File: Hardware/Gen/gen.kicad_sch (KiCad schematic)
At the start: 51 parts, among them J1 Screw_Terminal_01x03, J2 XLR4, J3 XLR3, J4 GAMEN, J5 SHORI, J6 MAE, J7 Screw_Terminal_01x02, U1 TPS56339DDCT, U3 TPS560430YDBVR

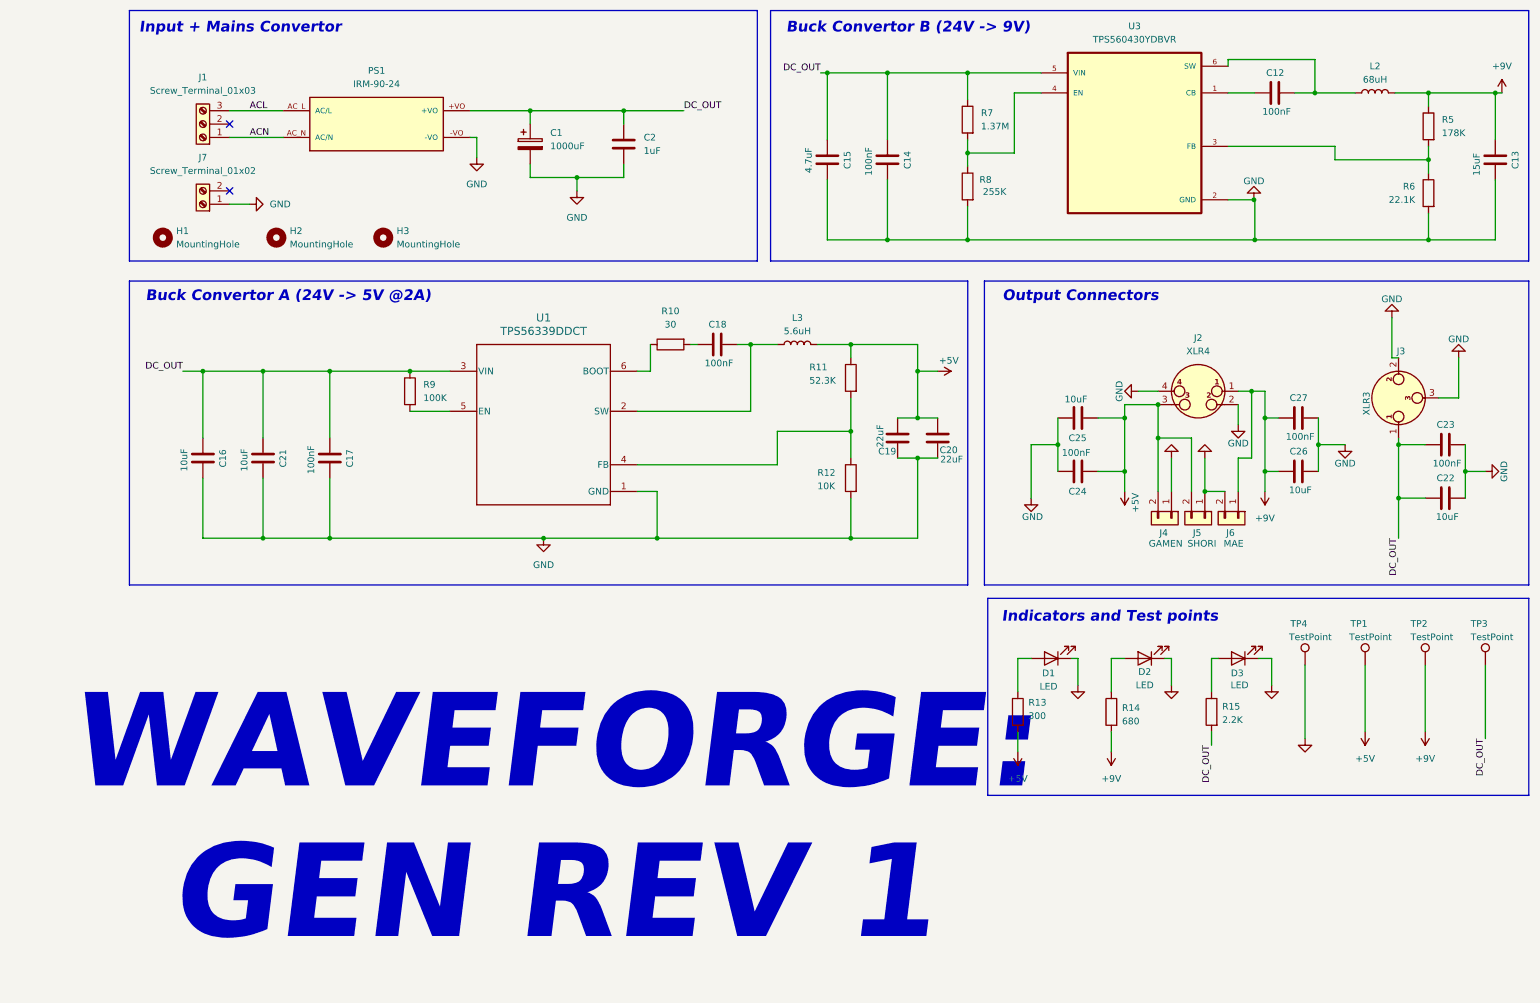
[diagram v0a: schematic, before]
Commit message: Gen: 5V buck convertor rework schems
Changed the 5V buck convertor to fgollow a ti chip with more of a max voltage headroom for safety.
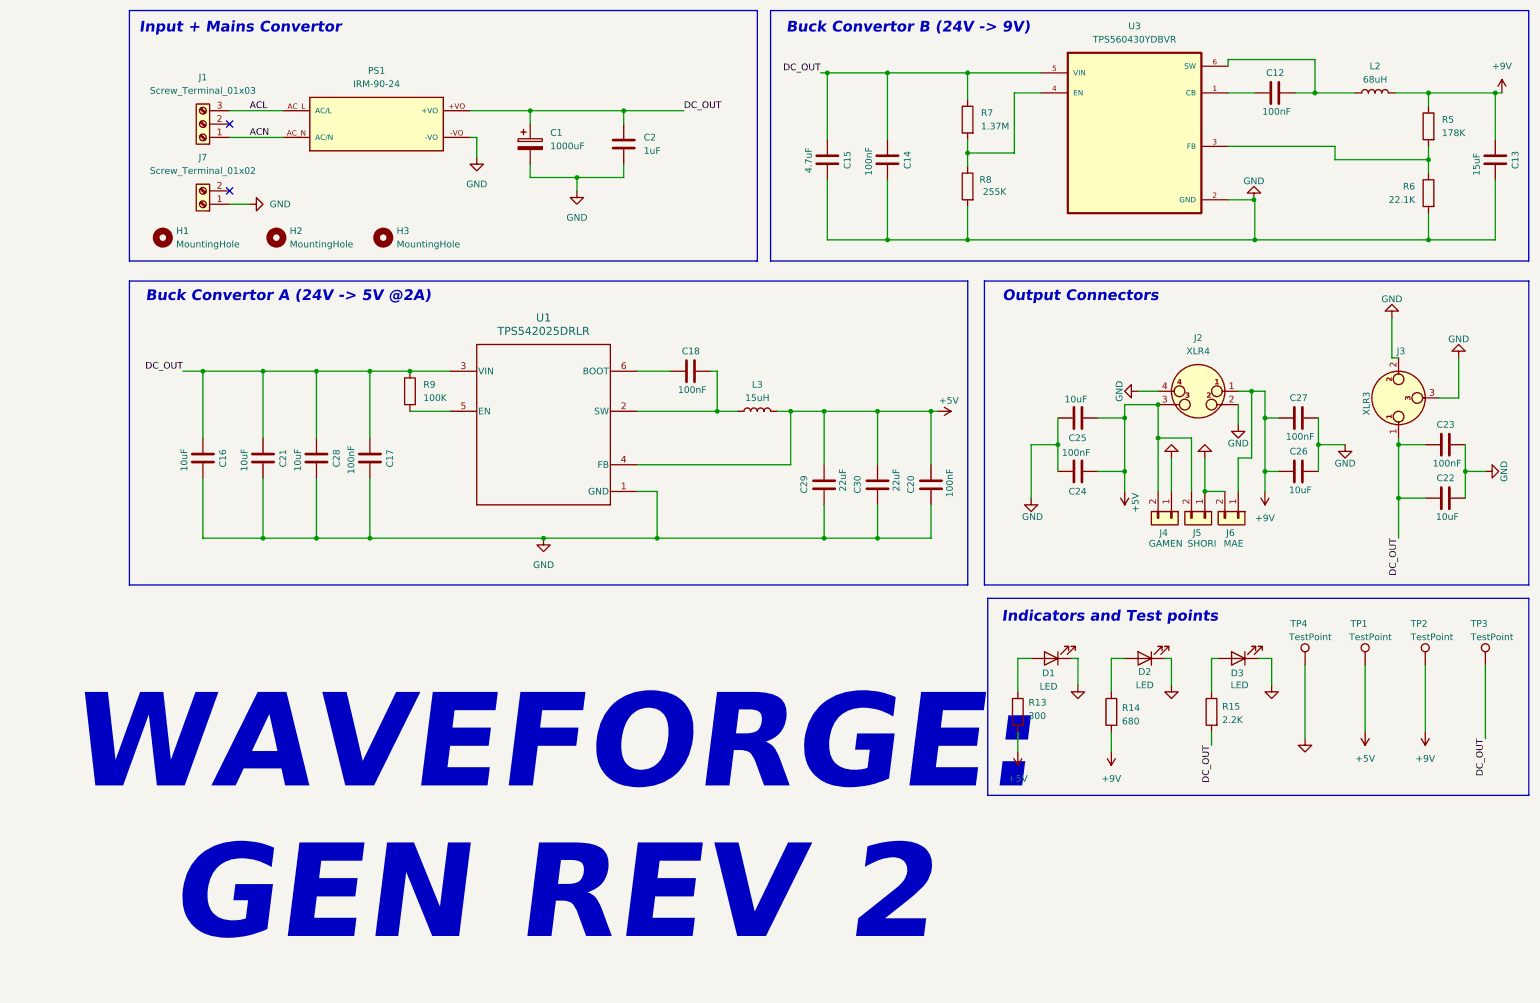
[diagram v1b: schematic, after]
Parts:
- removed C19: 22uF, Capacitor_SMD:C_0603_1608Metric_Pad1.08x0.95mm_HandSolder, symbol Device:C
- removed R10: 30, Resistor_SMD:R_0402_1005Metric_Pad0.72x0.64mm_HandSolder, symbol Device:R
- removed R11: 52.3K, Resistor_SMD:R_0603_1608Metric_Pad0.98x0.95mm_HandSolder, symbol Device:R
- removed R12: 10K, Resistor_SMD:R_0402_1005Metric_Pad0.72x0.64mm_HandSolder, symbol Device:R
- added C28: 10uF, Capacitor_SMD:C_0805_2012Metric_Pad1.18x1.45mm_HandSolder, symbol Device:C
- added C29, C30: 22uF, Capacitor_SMD:C_0805_2012Metric_Pad1.18x1.45mm_HandSolder, symbol Device:C
- C13, C16, C21, C22, C25, C26: footprint Capacitor_SMD:C_0603_1608Metric_Pad1.08x0.95mm_HandSolder -> Capacitor_SMD:C_0805_2012Metric_Pad1.18x1.45mm_HandSolder
- C20: value 22uF -> 100nF; footprint Capacitor_SMD:C_0603_1608Metric_Pad1.08x0.95mm_HandSolder -> Capacitor_SMD:C_0402_1005Metric_Pad0.74x0.62mm_HandSolder
- L3: value 5.6uH -> 15uH
- U1: value TPS56339DDCT -> TPS542025DRLR
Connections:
- net +5V: now also C20.1, U1.4 (FB), C29.1, C30.1; no longer C20.2
- net DC_OUT: now also C28.2
- net GND: now also C20.2, C28.1, C29.2, C30.2; no longer C20.1
- net at U1.6 (BOOT): now also C18.2
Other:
- note added: "WAVEFORGE: GEN REV 2"
- note removed: "WAVEFORGE: GEN REV 1"
- moved on the sheet: C17, C18, L3

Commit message: Gen: Barrel Jack Or-ing Circuit, and cart made
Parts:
- removed C21, C22, C28: 10uF, Capacitor_SMD:C_0805_2012Metric_Pad1.18x1.45mm_HandSolder, symbol Device:C
- removed C29, C30: 22uF, Capacitor_SMD:C_0805_2012Metric_Pad1.18x1.45mm_HandSolder, symbol Device:C
- removed TP3: TestPoint, TestPoint:TestPoint_Pad_D2.5mm, symbol Connector:TestPoint
- added C19: 82pF, Capacitor_SMD:C_0402_1005Metric_Pad0.74x0.62mm_HandSolder, symbol Device:C
- added D4, D5: B340, My FeetPics:DIOM5226X240N, symbol KiCad:B340
- added J9: PJ-051A, My FeetPics:CUI_PJ-051A, symbol My Symbols:PJ-051A
- added R10: 13.7K, Resistor_SMD:R_0402_1005Metric_Pad0.72x0.64mm_HandSolder, symbol Device:R
- C1: footprint Capacitor_THT:CP_Radial_D10.0mm_P5.00mm -> Capacitor_THT:CP_Radial_D13.0mm_P5.00mm
- C13: footprint Capacitor_SMD:C_0805_2012Metric_Pad1.18x1.45mm_HandSolder -> Capacitor_SMD:C_1206_3216Metric_Pad1.33x1.80mm_HandSolder
- C15: footprint Capacitor_SMD:C_0603_1608Metric_Pad1.08x0.95mm_HandSolder -> Capacitor_SMD:C_0805_2012Metric_Pad1.18x1.45mm_HandSolder
- C16: value 10uF -> 3.3uF
- C18, C20: value 100nF -> 47uF; footprint Capacitor_SMD:C_0402_1005Metric_Pad0.74x0.62mm_HandSolder -> Capacitor_SMD:C_1206_3216Metric
- C23: footprint Capacitor_SMD:C_0603_1608Metric_Pad1.08x0.95mm_HandSolder -> Capacitor_SMD:C_0402_1005Metric_Pad0.74x0.62mm_HandSolder
- L3: value 15uH -> 10uH; footprint My footprints:WE-XHMI_4040 -> My Footprints:IND_SRP6540-100M
- R13, R14: footprint Resistor_SMD:R_0402_1005Metric_Pad0.72x0.64mm_HandSolder -> Resistor_SMD:R_0805_2012Metric_Pad1.20x1.40mm_HandSolder
- R15: footprint Resistor_SMD:R_0805_2012Metric_Pad1.20x1.40mm_HandSolder -> Resistor_SMD:R_1206_3216Metric_Pad1.30x1.75mm_HandSolder
- R9: footprint Resistor_SMD:R_0603_1608Metric_Pad0.98x0.95mm_HandSolder -> Resistor_SMD:R_0402_1005Metric_Pad0.72x0.64mm_HandSolder
- U1: value TPS542025DRLR -> TPS543021DRLR; footprint Package_TO_SOT_SMD:SOT-23-6_Handsoldering -> Package_TO_SOT_SMD:SOT-563
- renumbered TP1 to 5V1, TP2 to 9V1, TP4 to GND1
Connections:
- net +5V: now also C18.2, C20.2, R9.1, C19.1; no longer C20.1, U1.4 (FB)
- net DC_OUT: now also U1.1 (VIN), D4.1 (K), D5.1 (K); no longer C17.2, PS1.+VO, R9.1, U1.3 (VIN)
- net GND: now also C18.1, C20.1, U1.3 (GND), J9.2, J9.3, J9.5 (SHIELD), J9.6 (SHIELD__1), R10.2; no longer C17.1, C20.2, U1.1 (GND)
- net at R9.2: now also U1.6 (FB), C19.2, R10.1; no longer U1.5 (EN)
- net at L3.2, U1.2 (SW): now also C17.1; no longer C18.1
- new net: D4.2 (A), PS1.+VO
- new net: C17.2, U1.4 (BOOT)
- new net: D5.2 (A), J9.1
- no-connect marks 2 -> 3
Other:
- moved on the sheet: C1, C16, C2, H1, H2, H3, J7

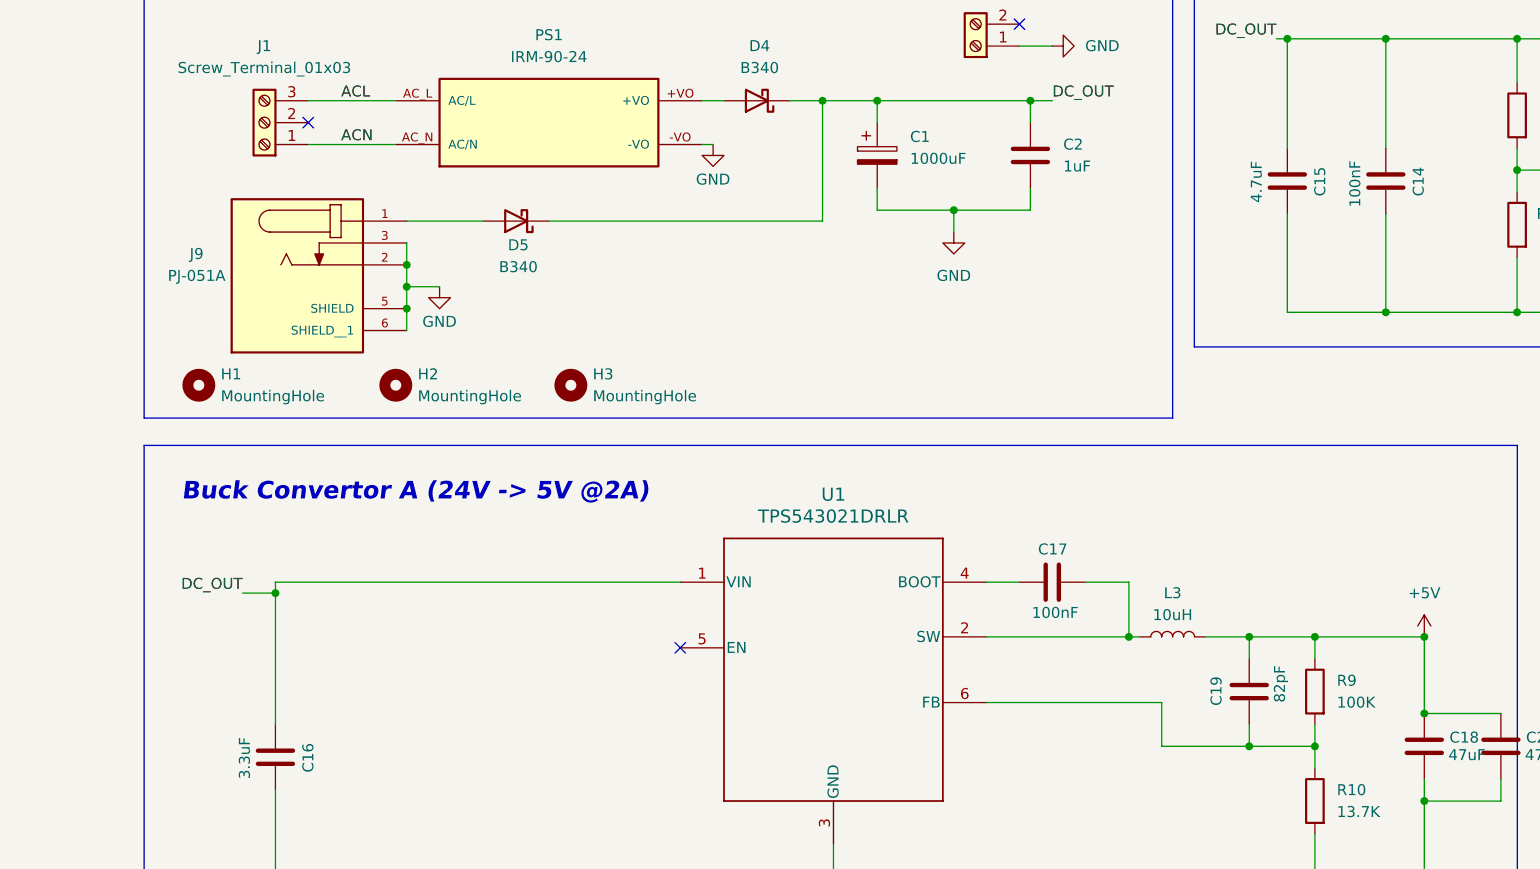
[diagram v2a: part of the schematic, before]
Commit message: added stiching vias on gen and changed SWD header on shori to header pins
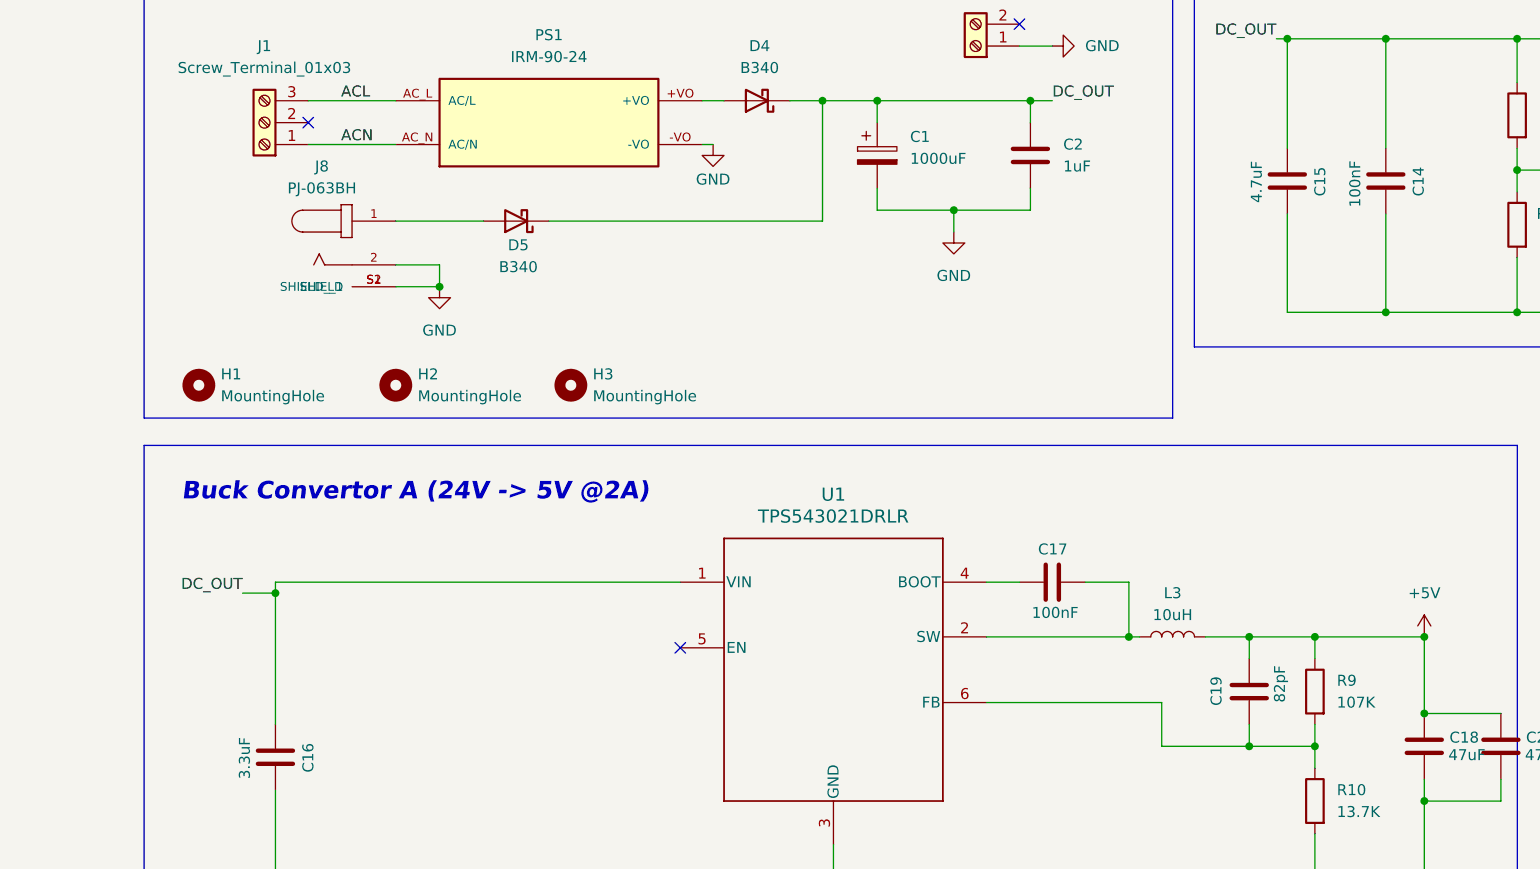
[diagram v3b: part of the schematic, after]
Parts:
- removed J9: PJ-051A, My FeetPics:CUI_PJ-051A, symbol My Symbols:PJ-051A
- added J8: PJ-063BH, My FeetPics:CUI_PJ-063BH, symbol My Symbols:PJ-063BH
- R9: value 100K -> 107K
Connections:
- net GND: now also J8.2, J8.S1 (SHIELD), J8.S2 (SHIELD__1)
- net at D5.2 (A): now also J8.1

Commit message: Gen rev 2 Ordered and Assembled. Proven Working All rails Spot on
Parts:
- removed J4: GAMEN, Connector_JST:JST_XH_S2B-XH-A_1x02_P2.50mm_Horizontal, symbol Connector_Generic:Conn_01x02
- added D10, D11, D7, D8: SMBJ6.0A, Diode_SMD:D_SMB, symbol KiCad:D
- added D6, D9: SMBJ28A, Diode_SMD:D_SMB, symbol KiCad:D
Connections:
- net +5V: now also D10.1 (K), D7.1 (K)
- net +9V: now also D11.1 (K), D8.1 (K)
- net DC_OUT: now also D9.1 (K)
- net GND: now also D10.2 (A), D11.2 (A), D6.2 (A), D7.2 (A), D8.2 (A), D9.2 (A)
- net at D5.2 (A), J8.1: now also D6.1 (K)
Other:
- moved on the sheet: D5
